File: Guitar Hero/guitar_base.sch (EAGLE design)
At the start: 5 parts

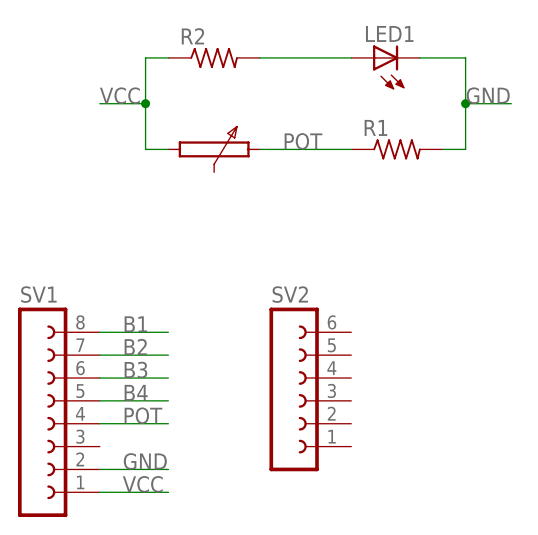
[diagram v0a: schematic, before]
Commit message: Added guitar base
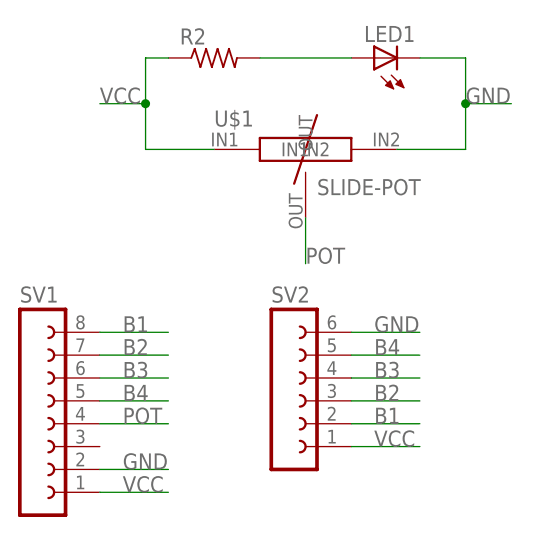
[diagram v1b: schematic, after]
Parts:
- removed R1: (no value), rcl:R-US_0207/7
- added U$1: SLIDE-POT, 319k:SLIDE-POT
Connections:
- net B1: now also SV2.2
- net B2: now also SV2.3
- net B3: now also SV2.4
- net B4: now also SV2.5
- net GND: now also SV2.6, U$1.IN2; no longer R1.2
- net POT: now also U$1.OUT; no longer R1.1
- net VCC: now also SV2.1, U$1.IN1
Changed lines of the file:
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@@
 </classes>
 <parts>
-<part name="R1" library="rcl" library_urn="urn:adsk.eagle:library:334" deviceset="R-US_" device="0207/7" package3d_urn="urn:adsk.eagle:package:23493/1"/>
 <part name="R2" library="rcl" library_urn="urn:adsk.eagle:library:334" deviceset="R-US_" device="0207/7" package3d_urn="urn:adsk.eagle:package:23493/1"/>
 <part name="LED1" library="led" library_urn="urn:adsk.eagle:library:259" deviceset="LED" device="5MM" package3d_urn="urn:adsk.eagle:package:15799/1"/>
 <part name="SV1" library="con-lsta" library_urn="urn:adsk.eagle:library:161" deviceset="FE08-1" device="" package3d_urn="urn:adsk.eagle:package:8194/1"/>
-<part name="P1" library="docu-dummy" library_urn="urn:adsk.eagle:library:215" deviceset="POT" device=""/>
 <part name="SV2" library="con-lsta" library_urn="urn:adsk.eagle:library:161" deviceset="FE06-1" device="" package3d_urn="urn:adsk.eagle:package:8191/1"/>
+<part name="U$1" library="319k" deviceset="SLIDE-POT" device=""/>
 </parts>
 <sheets>
@@
 </plain>
 <instances>
-<instance part="R1" gate="G$1" x="50.8" y="60.96"/>
 <instance part="R2" gate="G$1" x="30.48" y="71.12"/>
 <instance part="LED1" gate="G$1" x="48.26" y="71.12" rot="R90"/>
 <instance part="SV1" gate="G$1" x="10.16" y="30.48"/>
-<instance part="P1" gate="G$1" x="30.48" y="60.96" rot="R270"/>
 <instance part="SV2" gate="G$1" x="38.1" y="33.02"/>
+<instance part="U$1" gate="G$1" x="40.64" y="60.96"/>
 </instances>
 <busses>
@@
 <label x="20.32" y="40.64" size="1.778" layer="95"/>
 </segment>
+<segment>
+<pinref part="SV2" gate="G$1" pin="2"/>
+<wire x1="45.72" y1="30.48" x2="53.34" y2="30.48" width="0.1524" layer="91"/>
+<label x="48.26" y="30.48" size="1.778" layer="95"/>
+</segment>
 </net>
 <net name="B2" class="0">
@@
 <wire x1="17.78" y1="38.1" x2="25.4" y2="38.1" width="0.1524" layer="91"/>
 <label x="20.32" y="38.1" size="1.778" layer="95"/>
+</segment>
+<segment>
+<pinref part="SV2" gate="G$1" pin="3"/>
+<wire x1="45.72" y1="33.02" x2="53.34" y2="33.02" width="0.1524" layer="91"/>
+<label x="48.26" y="33.02" size="1.778" layer="95"/>
 </segment>
 </net>
@@
 <label x="20.32" y="35.56" size="1.778" layer="95"/>
 </segment>
+<segment>
+<pinref part="SV2" gate="G$1" pin="4"/>
+<wire x1="45.72" y1="35.56" x2="53.34" y2="35.56" width="0.1524" layer="91"/>
+<label x="48.26" y="35.56" size="1.778" layer="95"/>
+</segment>
 </net>
 <net name="B4" class="0">
@@
 <wire x1="17.78" y1="33.02" x2="25.4" y2="33.02" width="0.1524" layer="91"/>
 <label x="20.32" y="33.02" size="1.778" layer="95"/>
+</segment>
+<segment>
+<pinref part="SV2" gate="G$1" pin="5"/>
+<wire x1="45.72" y1="38.1" x2="53.34" y2="38.1" width="0.1524" layer="91"/>
+<label x="48.26" y="38.1" size="1.778" layer="95"/>
 </segment>
 </net>
@@
 </segment>
 <segment>
-<pinref part="R1" gate="G$1" pin="1"/>
-<wire x1="35.56" y1="60.96" x2="45.72" y2="60.96" width="0.1524" layer="91"/>
-<label x="38.1" y="60.96" size="1.778" layer="95"/>
+<pinref part="U$1" gate="G$1" pin="OUT"/>
+<wire x1="40.64" y1="53.34" x2="40.64" y2="48.26" width="0.1524" layer="91"/>
+<label x="40.64" y="48.26" size="1.778" layer="95"/>
 </segment>
 </net>
@@
 </segment>
 <segment>
-<pinref part="R1" gate="G$1" pin="2"/>
-<wire x1="55.88" y1="60.96" x2="58.42" y2="60.96" width="0.1524" layer="91"/>
 <wire x1="58.42" y1="60.96" x2="58.42" y2="66.04" width="0.1524" layer="91"/>
 <pinref part="LED1" gate="G$1" pin="C"/>
@@
 <junction x="58.42" y="66.04"/>
 <label x="58.42" y="66.04" size="1.778" layer="95"/>
+<pinref part="U$1" gate="G$1" pin="IN2"/>
+<wire x1="50.8" y1="60.96" x2="58.42" y2="60.96" width="0.1524" layer="91"/>
+</segment>
+<segment>
+<pinref part="SV2" gate="G$1" pin="6"/>
+<wire x1="45.72" y1="40.64" x2="53.34" y2="40.64" width="0.1524" layer="91"/>
+<label x="48.26" y="40.64" size="1.778" layer="95"/>
 </segment>
 </net>
@@
 <wire x1="22.86" y1="71.12" x2="22.86" y2="66.04" width="0.1524" layer="91"/>
 <wire x1="22.86" y1="66.04" x2="22.86" y2="60.96" width="0.1524" layer="91"/>
-<wire x1="22.86" y1="60.96" x2="25.4" y2="60.96" width="0.1524" layer="91"/>
 <wire x1="22.86" y1="66.04" x2="17.78" y2="66.04" width="0.1524" layer="91"/>
 <junction x="22.86" y="66.04"/>
 <label x="17.78" y="66.04" size="1.778" layer="95"/>
+<pinref part="U$1" gate="G$1" pin="IN1"/>
+<wire x1="22.86" y1="60.96" x2="30.48" y2="60.96" width="0.1524" layer="91"/>
+</segment>
+<segment>
+<pinref part="SV2" gate="G$1" pin="1"/>
+<wire x1="45.72" y1="27.94" x2="53.34" y2="27.94" width="0.1524" layer="91"/>
+<label x="48.26" y="27.94" size="1.778" layer="95"/>
 </segment>
 </net>

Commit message: Nano++ schematic; guitar hero redo to not use 1/64th bit
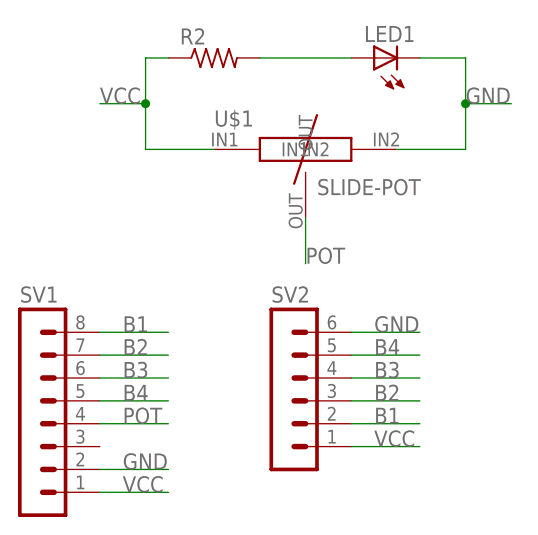
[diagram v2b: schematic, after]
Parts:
- SV1: device con-lsta:FE08-1 -> con-lstb:MA08-1
- SV2: device con-lsta:FE06-1 -> con-lstb:MA06-1
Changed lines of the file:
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@@
 <part name="R2" library="rcl" library_urn="urn:adsk.eagle:library:334" deviceset="R-US_" device="0207/7" package3d_urn="urn:adsk.eagle:package:23493/1"/>
 <part name="LED1" library="led" library_urn="urn:adsk.eagle:library:259" deviceset="LED" device="5MM" package3d_urn="urn:adsk.eagle:package:15799/1"/>
-<part name="SV1" library="con-lsta" library_urn="urn:adsk.eagle:library:161" deviceset="FE08-1" device="" package3d_urn="urn:adsk.eagle:package:8194/1"/>
-<part name="SV2" library="con-lsta" library_urn="urn:adsk.eagle:library:161" deviceset="FE06-1" device="" package3d_urn="urn:adsk.eagle:package:8191/1"/>
+<part name="SV1" library="con-lstb" library_urn="urn:adsk.eagle:library:162" deviceset="MA08-1" device="" package3d_urn="urn:adsk.eagle:package:8343/1"/>
+<part name="SV2" library="con-lstb" library_urn="urn:adsk.eagle:library:162" deviceset="MA06-1" device="" package3d_urn="urn:adsk.eagle:package:8340/1"/>
 <part name="U$1" library="319k" deviceset="SLIDE-POT" device=""/>
 </parts>
@@
 <instance part="R2" gate="G$1" x="30.48" y="71.12"/>
 <instance part="LED1" gate="G$1" x="48.26" y="71.12" rot="R90"/>
-<instance part="SV1" gate="G$1" x="10.16" y="30.48"/>
-<instance part="SV2" gate="G$1" x="38.1" y="33.02"/>
+<instance part="SV1" gate="1" x="10.16" y="30.48"/>
+<instance part="SV2" gate="1" x="38.1" y="35.56"/>
 <instance part="U$1" gate="G$1" x="40.64" y="60.96"/>
 </instances>
@@
 <net name="B1" class="0">
 <segment>
-<pinref part="SV1" gate="G$1" pin="8"/>
+<pinref part="SV1" gate="1" pin="8"/>
 <wire x1="17.78" y1="40.64" x2="25.4" y2="40.64" width="0.1524" layer="91"/>
 <label x="20.32" y="40.64" size="1.778" layer="95"/>
 </segment>
 <segment>
-<pinref part="SV2" gate="G$1" pin="2"/>
+<pinref part="SV2" gate="1" pin="2"/>
 <wire x1="45.72" y1="30.48" x2="53.34" y2="30.48" width="0.1524" layer="91"/>
 <label x="48.26" y="30.48" size="1.778" layer="95"/>
@@
 <net name="B2" class="0">
 <segment>
-<pinref part="SV1" gate="G$1" pin="7"/>
+<pinref part="SV1" gate="1" pin="7"/>
 <wire x1="17.78" y1="38.1" x2="25.4" y2="38.1" width="0.1524" layer="91"/>
 <label x="20.32" y="38.1" size="1.778" layer="95"/>
 </segment>
 <segment>
-<pinref part="SV2" gate="G$1" pin="3"/>
+<pinref part="SV2" gate="1" pin="3"/>
 <wire x1="45.72" y1="33.02" x2="53.34" y2="33.02" width="0.1524" layer="91"/>
 <label x="48.26" y="33.02" size="1.778" layer="95"/>
@@
 <net name="B3" class="0">
 <segment>
-<pinref part="SV1" gate="G$1" pin="6"/>
+<pinref part="SV1" gate="1" pin="6"/>
 <wire x1="17.78" y1="35.56" x2="25.4" y2="35.56" width="0.1524" layer="91"/>
 <label x="20.32" y="35.56" size="1.778" layer="95"/>
 </segment>
 <segment>
-<pinref part="SV2" gate="G$1" pin="4"/>
+<pinref part="SV2" gate="1" pin="4"/>
 <wire x1="45.72" y1="35.56" x2="53.34" y2="35.56" width="0.1524" layer="91"/>
 <label x="48.26" y="35.56" size="1.778" layer="95"/>
@@
 <net name="B4" class="0">
 <segment>
-<pinref part="SV1" gate="G$1" pin="5"/>
+<pinref part="SV1" gate="1" pin="5"/>
 <wire x1="17.78" y1="33.02" x2="25.4" y2="33.02" width="0.1524" layer="91"/>
 <label x="20.32" y="33.02" size="1.778" layer="95"/>
 </segment>
 <segment>
-<pinref part="SV2" gate="G$1" pin="5"/>
+<pinref part="SV2" gate="1" pin="5"/>
 <wire x1="45.72" y1="38.1" x2="53.34" y2="38.1" width="0.1524" layer="91"/>
 <label x="48.26" y="38.1" size="1.778" layer="95"/>
@@
 <net name="POT" class="0">
 <segment>
-<pinref part="SV1" gate="G$1" pin="4"/>
+<pinref part="SV1" gate="1" pin="4"/>
 <wire x1="17.78" y1="30.48" x2="25.4" y2="30.48" width="0.1524" layer="91"/>
 <label x="20.32" y="30.48" size="1.778" layer="95"/>
 </segment>
 <segment>
-<pinref part="U$1" gate="G$1" pin="OUT"/>
 <wire x1="40.64" y1="53.34" x2="40.64" y2="48.26" width="0.1524" layer="91"/>
 <label x="40.64" y="48.26" size="1.778" layer="95"/>
+<pinref part="U$1" gate="G$1" pin="OUT"/>
 </segment>
 </net>
 <net name="GND" class="0">
 <segment>
-<pinref part="SV1" gate="G$1" pin="2"/>
+<pinref part="SV1" gate="1" pin="2"/>
 <wire x1="17.78" y1="25.4" x2="25.4" y2="25.4" width="0.1524" layer="91"/>
 <label x="20.32" y="25.4" size="1.778" layer="95"/>
@@
 <junction x="58.42" y="66.04"/>
 <label x="58.42" y="66.04" size="1.778" layer="95"/>
+<wire x1="50.8" y1="60.96" x2="58.42" y2="60.96" width="0.1524" layer="91"/>
 <pinref part="U$1" gate="G$1" pin="IN2"/>
-<wire x1="50.8" y1="60.96" x2="58.42" y2="60.96" width="0.1524" layer="91"/>
 </segment>
 <segment>
-<pinref part="SV2" gate="G$1" pin="6"/>
+<pinref part="SV2" gate="1" pin="6"/>
 <wire x1="45.72" y1="40.64" x2="53.34" y2="40.64" width="0.1524" layer="91"/>
 <label x="48.26" y="40.64" size="1.778" layer="95"/>
@@
 <net name="VCC" class="0">
 <segment>
-<pinref part="SV1" gate="G$1" pin="1"/>
+<pinref part="SV1" gate="1" pin="1"/>
 <wire x1="17.78" y1="22.86" x2="25.4" y2="22.86" width="0.1524" layer="91"/>
 <label x="20.32" y="22.86" size="1.778" layer="95"/>
@@
 <junction x="22.86" y="66.04"/>
 <label x="17.78" y="66.04" size="1.778" layer="95"/>
+<wire x1="22.86" y1="60.96" x2="30.48" y2="60.96" width="0.1524" layer="91"/>
 <pinref part="U$1" gate="G$1" pin="IN1"/>
-<wire x1="22.86" y1="60.96" x2="30.48" y2="60.96" width="0.1524" layer="91"/>
 </segment>
 <segment>
-<pinref part="SV2" gate="G$1" pin="1"/>
+<pinref part="SV2" gate="1" pin="1"/>
 <wire x1="45.72" y1="27.94" x2="53.34" y2="27.94" width="0.1524" layer="91"/>
 <label x="48.26" y="27.94" size="1.778" layer="95"/>
